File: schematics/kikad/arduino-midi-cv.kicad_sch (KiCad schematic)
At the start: 14 parts, among them J1 V/oct OUT, J2 GATE OUT, Q1 BC548

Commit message: Update schematics
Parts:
- removed A?: Arduino_UNO_R3, Module:Arduino_UNO_R3, symbol MCU_Module:Arduino_UNO_R3
- removed C1, C2: 1uF, symbol Device:C_Polarized
- removed D1: GATE LED, LED_THT:LED_D5.0mm, symbol Device:LED
- removed J1: V/oct OUT, symbol Connector:AudioJack2
- removed Q1: BC548, Package_TO_SOT_THT:TO-92_Inline, symbol Transistor_BJT:BC548
- removed R1, R2, R3, R7: 1k, symbol Device:R_US
- removed R4: 2k, symbol Device:R_US
- removed R5: 5k1, symbol Device:R_US
- added A?: Arduino_Nano_v3.x, Module:Arduino_Nano, symbol MCU_Module:Arduino_Nano_v3.x
- added C? (x8): 100nF, Capacitor_THT:C_Disc_D3.0mm_W1.6mm_P2.50mm, symbol Device:C
- added C? (x2): 10uF, symbol Device:C_Polarized_US
- added D1: 1N4148, Diode_THT:D_DO-35_SOD27_P7.62mm_Horizontal, symbol Diode:1N4148
- added D? (x2): BAT43, Diode_THT:D_DO-35_SOD27_P7.62mm_Horizontal, symbol Diode:BAT43
- added D?: GATE LED, LED_THT:LED_D5.0mm, symbol Device:LED
- added D? (x2): 1N4001, Diode_THT:D_DO-41_SOD81_P10.16mm_Horizontal, symbol Diode:1N4001
- added J3: Bend Out, symbol Connector:AudioJack2
- added J?: MOD WHEEL, symbol Connector:AudioJack2
- added J?: Velocity, symbol Connector:AudioJack2
- added J?: V/oct OUT, symbol Connector:AudioJack2
- added J_MIDI_OUT, J_MIDI_THRU?: DIN-5_180degree, Connector_PinHeader_1.00mm:PinHeader_1x05_P1.00mm_Vertical, symbol Connector:DIN-5_180degree
- added LED_Bend? (x2), LED_MOD, LED_V/oct, LED_VELOCITY: LED, LED_THT:LED_D5.0mm, symbol Device:LED
- added Q? (x2): BC548, Package_TO_SOT_THT:TO-92L_Inline_Wide, symbol Transistor_BJT:BC548
- added R11, R? (x8): 1k, symbol Device:R_US
- added R12, R? (x2): 220R, symbol Device:R_US
- added R13: 2K, symbol Device:R_US
- added R8, R? (x7): 10k, symbol Device:R_US
- added R? (x2): 10R, symbol Device:R_US
- added R? (x4): 100k, symbol Device:R_US
- added R?: 2k, symbol Device:R_US
- added R?: 3.3k, symbol Device:R_US
- added RV?: 10k, symbol Device:R_Potentiometer_Trim_US
- added U? (x5): TL074, symbol Amplifier_Operational:TL074
- added U?: 6N137, Package_DIP:DIP-8_W7.62mm, symbol Isolator:6N137
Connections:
- net +5V: now also A?.27 (+5V), C?.1, D?.1 (K), R13.2, R?.1, R?.2, U?.8 (VCC)
- net Earth: now also A?.29 (GND), C?.1, C?.1, C?.2, C?.2, C?.2, C?.2, C?.2, C?.2, C?.2, C?.2, D?.1 (K), D?.1 (K), D?.2 (A), D?.2 (A), J3.S, J?.S, J?.S, J?.S, J_MIDI_THRU?.2, LED_Bend?.1 (K), LED_Bend?.2 (A), LED_MOD.1 (K), LED_V/oct.1 (K), LED_VELOCITY.1 (K), Q?.3 (E), Q?.3 (E), R?.1, R?.1, RV?.1, U?.5 (GND)
- net at R6.1: now also A?.15 (D12), D?.1 (K), D?.2 (A), R?.1
- new net: J?.T, R?.2 (x3)
- new net: R?.1, R?.2, U?.1
- new net: C?.1, R?.2, U?.10 (+)
- new net: R?.1, U?.8, U?.9 (-)
- new net: D?.2 (A), R?.2
- new net: C?.1, R?.2, U?.5 (+)
- new net: R?.1, R?.2, U?.6 (-)
- new net: R11.1, R?.1, R?.2, U?.7
- new net: Q?.2 (B), R?.1 (x2)
- new net: Q?.1 (C), R?.1, R?.2
- new net: R?.1, RV?.2
- new net: A?.13 (D10), R?.1
- new net: LED_MOD.2 (A), R?.1
- new net: C?.1, R?.2, U?.3 (+)
- new net: R?.1, R?.2, U?.13 (-)
- new net: R?.1, R?.2, U?.14
- new net: J3.T, R11.2
- new net: C?.1, R8.2, U?.12 (+)
- new net: J_MIDI_THRU?.5, R?.1
- new net: Q?.1 (C), R?.2
- new net: C?.1, R?.1, R?.2
- new net: A?.2 (D0/RX), R13.1, R?.2, U?.6 (VO)
- new net: LED_Bend?.1 (K), LED_Bend?.2 (A), R?.2
- new net: R?.1, R?.2, U?.2 (-)
- new net: LED_V/oct.2 (A), R?.1
- new net: D1.1 (K), R12.2, U?.2 (A)
- new net: D1.2 (A), J_MIDI_OUT.5, U?.3 (C)
- new net: J_MIDI_THRU?.4, R?.2
- new net: J_MIDI_OUT.4, R12.1
- new net: LED_VELOCITY.2 (A), R?.1
- new net +12V: A?.30 (VIN), C?.1, C?.1, D?.1 (K), R?.1, U?.4 (V+)
- new net -12V: C?.2, C?.2, D?.2 (A), R?.1, RV?.3, U?.11 (V-)
- new net -12V In: R?.2
- new net 12V In: R?.2
- new net Mod LED: A?.14 (D11), R8.1, R?.2
- new net Velocity LED: A?.6 (D3), R?.1, R?.2
- new net V/oct LED: A?.12 (D9), R?.1, R?.2
- no-connect marks 0 -> 6
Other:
- note removed: "TODO: reconsider if this transitor is realy nessesery"
- note removed: "or any other signal NPN BJT"
- moved on the sheet: J2, R6

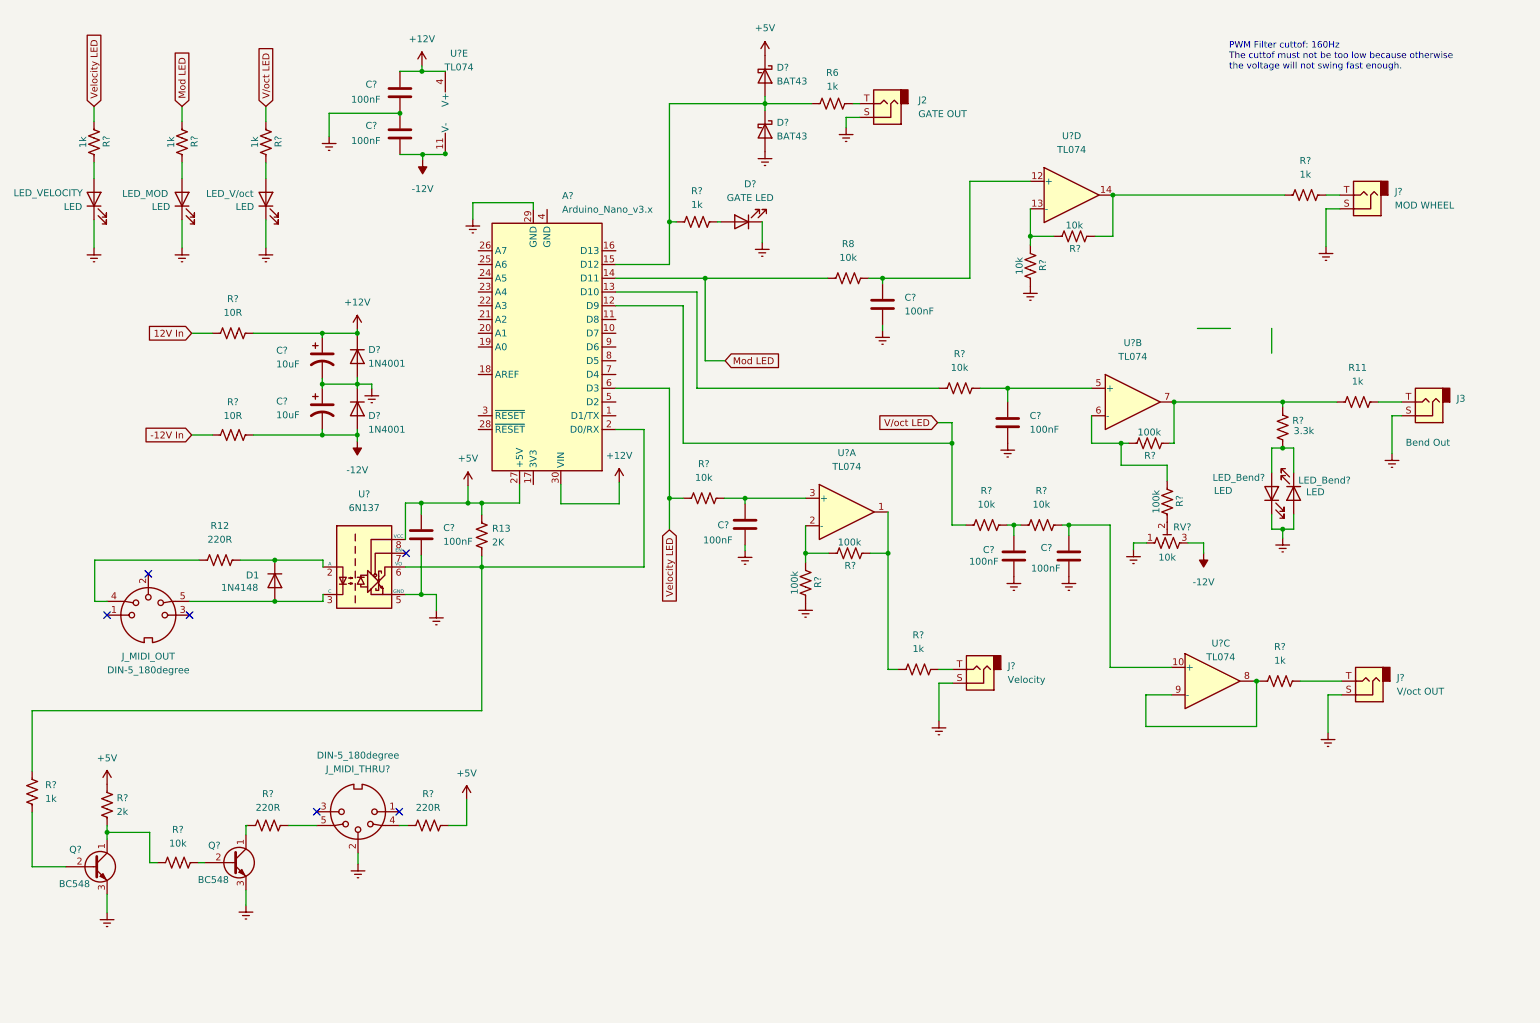
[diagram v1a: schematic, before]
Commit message: Redraw schematics to be more butiful
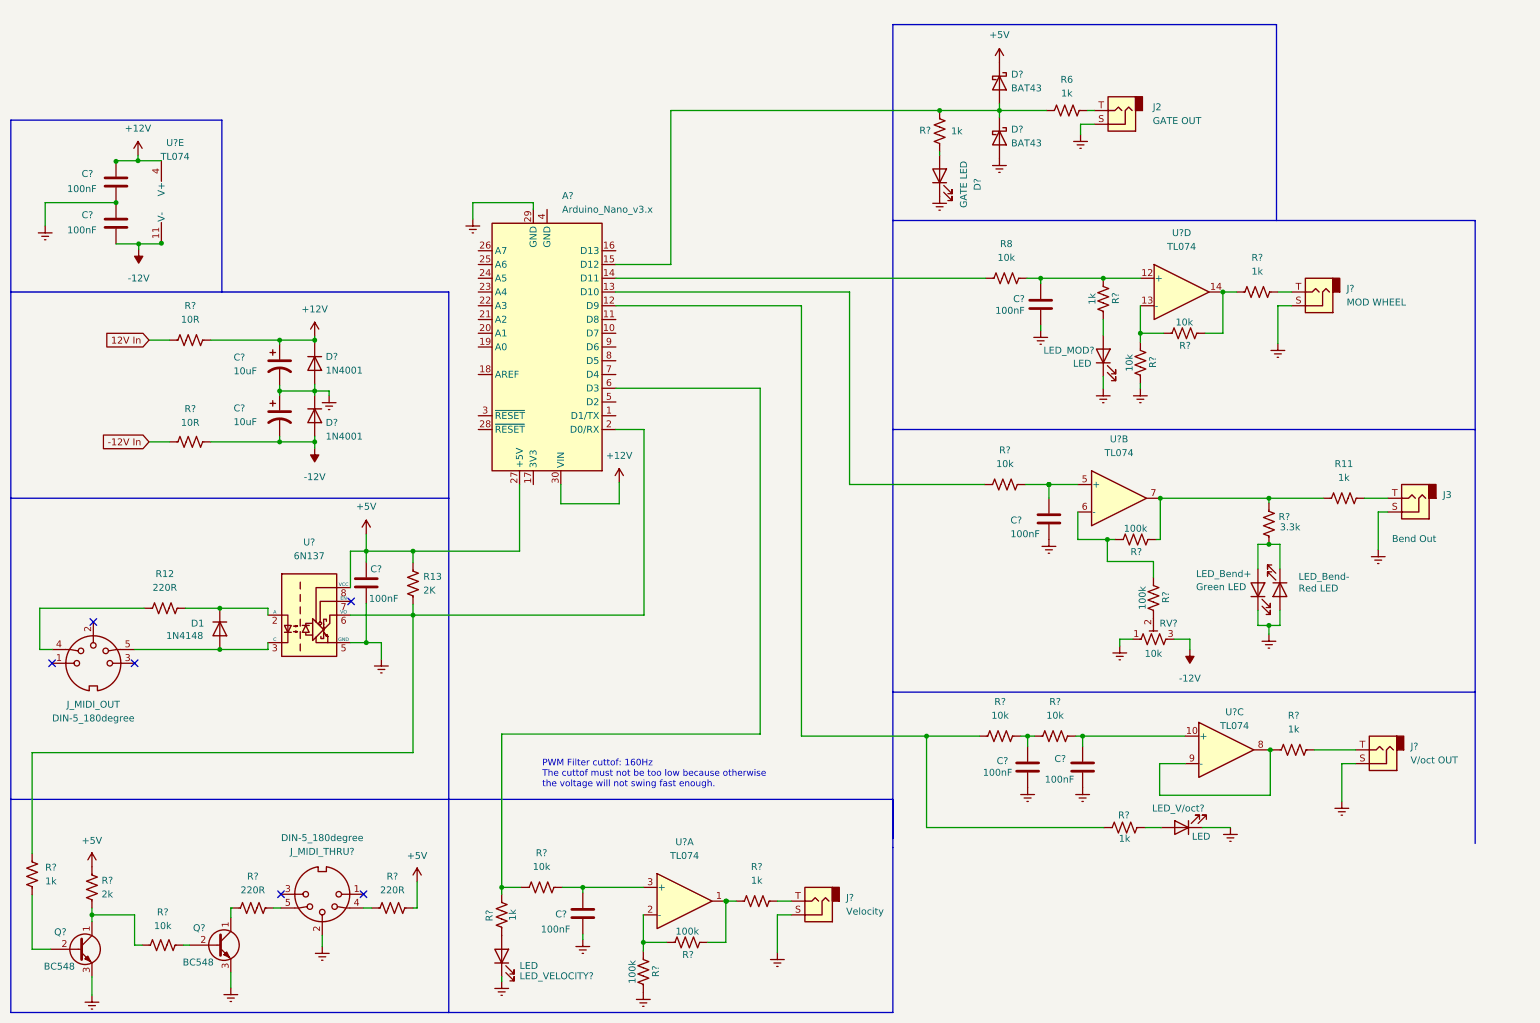
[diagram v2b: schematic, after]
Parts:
- removed D?: GATE LED, LED_THT:LED_D5.0mm, symbol Device:LED
- removed LED_MOD, LED_V/oct, LED_VELOCITY: LED, LED_THT:LED_D5.0mm, symbol Device:LED
- removed R? (x4): 1k, symbol Device:R_US
- added D?: GATE LED, LED_THT:LED_D5.0mm, symbol Device:LED
- added LED_MOD?, LED_V/oct?, LED_VELOCITY?: LED, LED_THT:LED_D5.0mm, symbol Device:LED
- added R? (x4): 1k, symbol Device:R_US
- LED_Bend+: renamed from LED_Bend?; value LED -> Green LED
- LED_Bend-: renamed from LED_Bend?; value LED -> Red LED
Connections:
- net Earth: now also D?.1 (K), LED_MOD?.1 (K), LED_V/oct?.1 (K), LED_VELOCITY?.1 (K)
- net at A?.15 (D12), D?.1 (K), D?.2 (A)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: now also R?.1
- net at C?.1, R8.2, U?.12 (+): now also R?.2
- net Mod LED: no longer names the net of A?.14 (D11), R8.1
- net Velocity LED: no longer names the net of A?.6 (D3), R?.1
- net Velocity LED: now also R?.1
- net V/oct LED: no longer names the net of A?.12 (D9), R?.1
- net V/oct LED: now also R?.2
- new net: D?.2 (A), R?.2
- new net: LED_V/oct?.2 (A), R?.1
- new net: LED_VELOCITY?.2 (A), R?.2
- new net: LED_MOD?.2 (A), R?.1
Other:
- moved on the sheet: C?, D1, D?, J2, J3, J?, J_MIDI_OUT, J_MIDI_THRU?, LED_Bend+, LED_Bend-, Q?, R11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

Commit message: Start PCB
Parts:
- C3, C4: renamed from C?; footprint (none) -> Capacitor_THT:CP_Radial_D5.0mm_P2.50mm
- D2, D3: renamed from D?; footprint Diode_THT:D_DO-41_SOD81_P10.16mm_Horizontal -> Diode_THT:D_DO-41_SOD81_P2.54mm_Vertical_AnodeUp
- J1, J4, J5: renamed from J?; footprint (none) -> Connector_PinHeader_1.00mm:PinHeader_1x02_P1.00mm_Vertical
- J2, J3: footprint (none) -> Connector_PinHeader_1.00mm:PinHeader_1x02_P1.00mm_Vertical
- R1, R10, R14, R15, R17, R18, R19, R2, R20, R21, R22, R23, R26, R28, R29, R3, R30, R4, R5, R7, R9: renamed from R?; footprint (none) -> Resistor_THT:R_Axial_DIN0207_L6.3mm_D2.5mm_P10.16mm_Horizontal
- R11, R12, R13, R6, R8: footprint (none) -> Resistor_THT:R_Axial_DIN0207_L6.3mm_D2.5mm_P10.16mm_Horizontal
- R16, R24: renamed from R?; footprint (none) -> Resistor_THT:R_Axial_DIN0207_L6.3mm_D2.5mm_P2.54mm_Vertical
- R25: renamed from R?; value 10k -> 100k; footprint (none) -> Resistor_THT:R_Axial_DIN0207_L6.3mm_D2.5mm_P10.16mm_Horizontal
- R27: renamed from R?; value 10k -> 100k; footprint (none) -> Resistor_THT:R_Axial_DIN0207_L6.3mm_D2.5mm_P2.54mm_Vertical
- RV1: renamed from RV?; footprint (none) -> Potentiometer_THT:Potentiometer_ACP_CA9-V10_Vertical
- U1: renamed from U?; footprint (none) -> Package_DIP:DIP-14_W7.62mm_Socket
- gave numbers to parts that had none: 19
- renumbered J_MIDI_OUT to J_MIDI_OUT1, LED_Bend+ to LED_Bend+1, LED_Bend- to LED_Bend-1

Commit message: There has been some work done, a long time a go I have no idea what
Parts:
- removed LED_Bend+1: Green LED, LED_THT:LED_D5.0mm, symbol Device:LED
- removed LED_Bend-1: Red LED, LED_THT:LED_D5.0mm, symbol Device:LED
- removed R4, R5: 10R, Resistor_THT:R_Axial_DIN0207_L6.3mm_D2.5mm_P10.16mm_Horizontal, symbol Device:R_US
- added C11, C12: 100nF, Capacitor_THT:C_Disc_D3.0mm_W1.6mm_P2.50mm, symbol Device:C
- added C?: 10uf, Capacitor_THT:CP_Radial_D5.0mm_P2.50mm, symbol Device:C_Polarized_US
- added FB1, FB2: FerriteBead, Resistor_THT:R_Axial_DIN0207_L6.3mm_D2.5mm_P10.16mm_Horizontal, symbol Device:FerriteBead
- added J6: Power connector, Connector_JST:JST_XH_B5B-XH-A_1x05_P2.50mm_Vertical, symbol Connector:Conn_01x05_Male
- added J7: Eurorack power connector, Connector_IDC:IDC-Header_2x08_P2.54mm_Vertical, symbol Connector:Conn_01x16_Male
- added LED_Bend1: LED_RG, LED_THT:LED_D5.0mm, symbol Device:LED_Dual_Bidirectional
- added R32: 220, Resistor_SMD:R_0805_2012Metric_Pad1.20x1.40mm_HandSolder, symbol Device:R_US
- added R33: 1k, Resistor_THT:R_Axial_DIN0207_L6.3mm_D2.5mm_P10.16mm_Horizontal, symbol Device:R_US
- added SW1: RotaryEncoder_Switch, Rotary_Encoder:RotaryEncoder_Alps_EC11E-Switch_Vertical_H20mm, symbol Device:RotaryEncoder_Switch
- added U3: OLED_Display_SPI, Dr_McFishs_misc_footprints:SPI Oled dislay SH1106, symbol Dr_McFishs_misc_symbols:OLED_Display_SPI
- C3, C4: value 10uF -> 22uF
- D1: footprint Diode_THT:D_DO-35_SOD27_P7.62mm_Horizontal -> Diode_THT:D_DO-35_SOD27_P2.54mm_Vertical_AnodeUp
- D2, D3: footprint Diode_THT:D_DO-41_SOD81_P2.54mm_Vertical_AnodeUp -> Diode_THT:D_DO-41_SOD81_P12.70mm_Horizontal
- J1, J2, J3, J4, J5: footprint Connector_PinHeader_1.00mm:PinHeader_1x02_P1.00mm_Vertical -> Library:Jack breakcout cables
- J_MIDI_OUT1, J_MIDI_THRU1: footprint Connector_PinHeader_1.00mm:PinHeader_1x05_P1.00mm_Vertical -> Library:SIP-2
- Q1, Q2: footprint Package_TO_SOT_THT:TO-92L_Inline_Wide -> Package_TO_SOT_THT:TO-92_Inline
- R12, R25: footprint Resistor_THT:R_Axial_DIN0207_L6.3mm_D2.5mm_P10.16mm_Horizontal -> Resistor_THT:R_Axial_DIN0207_L6.3mm_D2.5mm_P2.54mm_Vertical
- R13: footprint Resistor_THT:R_Axial_DIN0207_L6.3mm_D2.5mm_P10.16mm_Horizontal -> Resistor_THT:R_Axial_DIN0207_L6.3mm_D2.5mm_P7.62mm_Horizontal
- R3: value 10k -> 1k
- RV1: footprint Potentiometer_THT:Potentiometer_ACP_CA9-V10_Vertical -> Potentiometer_THT:Potentiometer_Bourns_3296W_Vertical
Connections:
- net +12V: now also FB1.2, R32.2; no longer A1.30 (VIN)
- net +5V: now also J7.11 (Pin_11), J7.12 (Pin_12), U3.2 (VDD)
- net -12V: now also FB2.2
- net -12V In: now also FB2.1, J6.5 (Pin_5), J7.1 (Pin_1), J7.2 (Pin_2)
- net 12V In: now also FB1.1, J6.1 (Pin_1), J7.10 (Pin_10), J7.9 (Pin_9)
- net Earth: now also C11.2, C12.2, C?.2, J6.2 (Pin_2), J6.3 (Pin_3), J6.4 (Pin_4), J7.3 (Pin_3), J7.4 (Pin_4), J7.5 (Pin_5), J7.6 (Pin_6), J7.7 (Pin_7), J7.8 (Pin_8), LED_Bend1.2 (AK), SW1.C, SW1.S2, U3.1 (GND)
- net at D5.2 (A), D6.1 (K), R6.1: now also R33.2; no longer A1.15 (D12), R18.1
- net Gate  Out: now reaches J2.T, R6.2
- net Gate  Out: now also J7.15 (Pin_15), J7.16 (Pin_16)
- net Pitch Wheel PWM: now reaches A1.13 (D10), R20.1
- net at C8.1, R8.2, U1.12 (+): no longer R22.2
- net V/oct  Out: now reaches J5.T, R30.2
- net V/oct  Out: now also J7.13 (Pin_13), J7.14 (Pin_14)
- net V/oct PWM: now reaches A1.12 (D9), R19.1, R23.2
- net Velocity PWM: now reaches R10.1, R14.1
- net Velocity PWM: now also A1.8 (D5); no longer A1.6 (D3)
- net MIDI RX: now reaches A1.2 (D0/RX), R1.2, R13.1, U2.6 (VO)
- net at R29.2: now also LED_Bend1.1 (KA)
- net SPI Reset: now reaches A1.1 (D1/TX)
- net SPI Reset: now also U3.5 (RES)
- net SPI DC: now reaches A1.10 (D7)
- net SPI DC: now also U3.6 (DC)
- net SPI CS: now reaches A1.11 (D8)
- net SPI CS: now also U3.7 (CS)
- net Mod Wheel PWM: now reaches R8.1
- net Mod Wheel PWM: now also A1.9 (D6), R22.2; no longer A1.14 (D11)
- net SPI SLK: now reaches A1.16 (D13)
- net SPI SLK: now also U3.3 (SCK)
- net Encoder Button: now reaches A1.22 (A3)
- net Encoder Button: now also SW1.S1
- net Encoder CLK: now reaches A1.5 (D2)
- net Encoder CLK: now also C12.1, SW1.B
- net Gate Pin: now reaches A1.7 (D4)
- net Gate Pin: now also R18.1, R33.1
- new net: A1.30 (VIN), C?.1, R32.1
- new net Encoder DT: A1.6 (D3), C11.1, SW1.A
- new net SPI MOSI: A1.14 (D11), U3.4 (SDA)
- no-connect marks 6 -> 19
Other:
- moved on the sheet: A1, C10, C3, C4, C7, C8, D2, D3, D5, D6, J2, J4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
